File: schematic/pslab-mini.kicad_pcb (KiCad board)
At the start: 4 copper layers, 85 x 56 mm, 145 parts, among them J2 BAT, J3 Conn_Coaxial, J4 Conn_Coaxial, J5 Conn_02x16_Odd_Even, J6 Conn_01x15_Socket, J7 Conn_02x03_Top_Bottom, J8 USB_C_Receptacle_USB2.0_16P, Q1 MMBT3904, Q2 MMBT3906, SW1 Reset, SW2 Power, U1 MT2496, U10 TL082, U11 ESP32-C3, U12 IP5189T, U2 AP3015A, U4 SP0503BAHT, U5 AMS1117-3.3, U6 STM32H563RIT6, U7 TL082, U8 MCP6S21, U9 MCP6S21, X1 32kHz768, Y1 Crystal_25MHz, Y2 Crystal_40Mhz

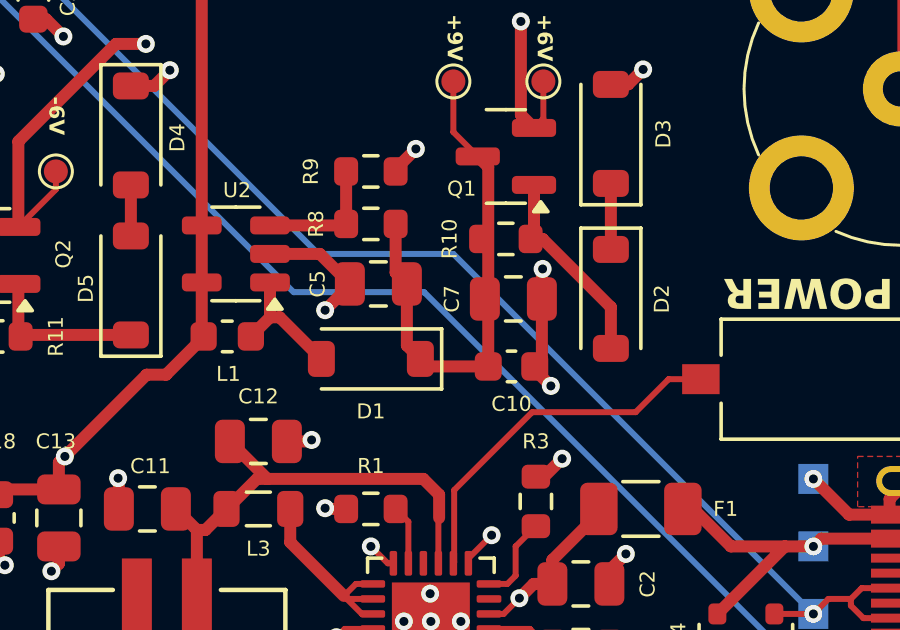
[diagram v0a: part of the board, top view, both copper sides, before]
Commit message: fix: wrong capacitor placement in voltage doubler
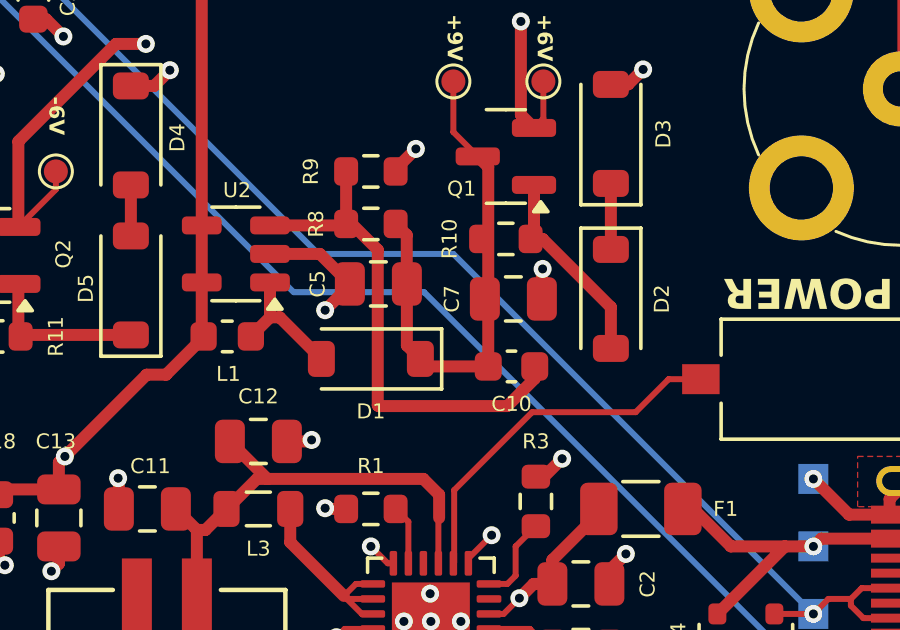
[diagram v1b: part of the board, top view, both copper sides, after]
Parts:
- D1: value K1N5817HW-7-F -> K1N5817HW
- D3: value 6.8V -> 6v8
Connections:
- C10 pad 2: GND -> Net-(U2-FB)
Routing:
- net Net-(U2-FB): track 4.31 -> 17.4 mm
- net GND: track 122.4 -> 119.2 mm, vias 84 -> 83

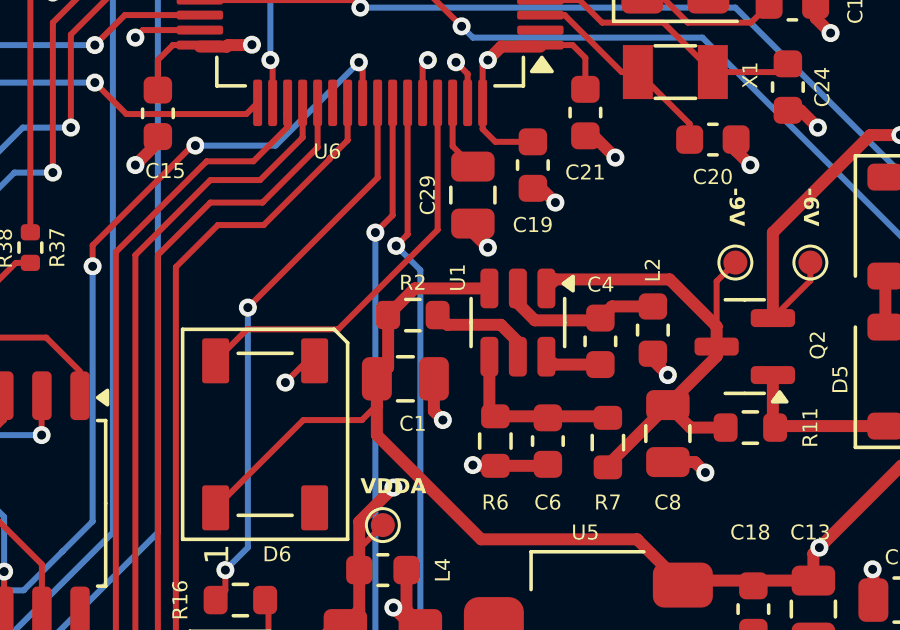
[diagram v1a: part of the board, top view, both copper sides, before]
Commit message: fix: schematic placement of voltage inverter block
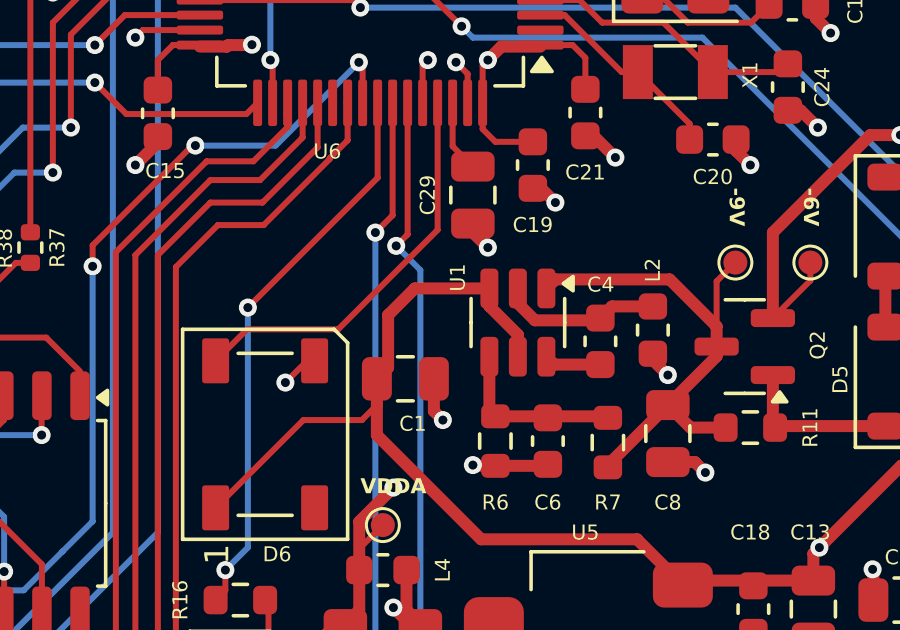
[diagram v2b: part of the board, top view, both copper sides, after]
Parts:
- removed R2: 200k, Resistor_SMD:R_0603_1608Metric
- D4: value 6.8V -> 6v8
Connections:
- U1 pad 5: Net-(U1-EN) -> +5V
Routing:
- net Net-(U1-EN): track 3.54 -> 0.00 mm
- net +5V: track 88.8 -> 91.5 mm

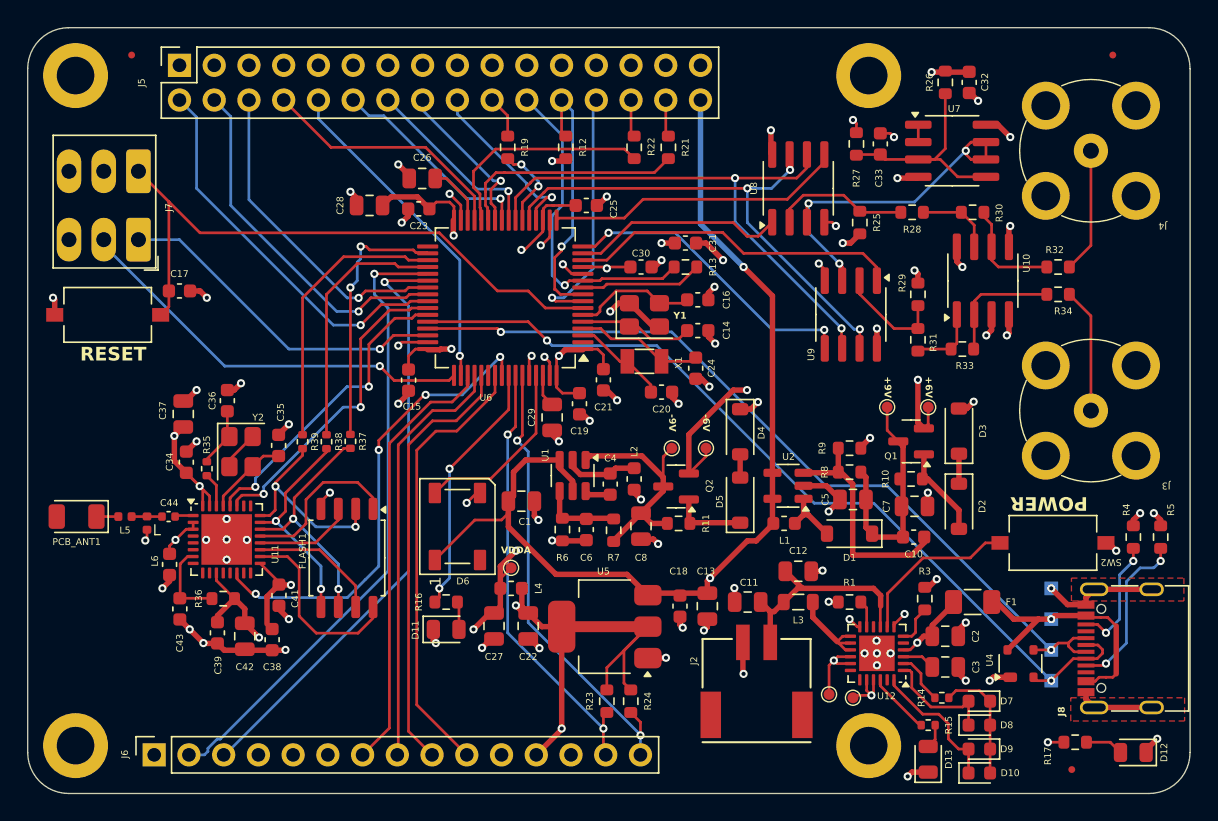
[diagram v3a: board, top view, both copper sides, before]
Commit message: Updated differential routing
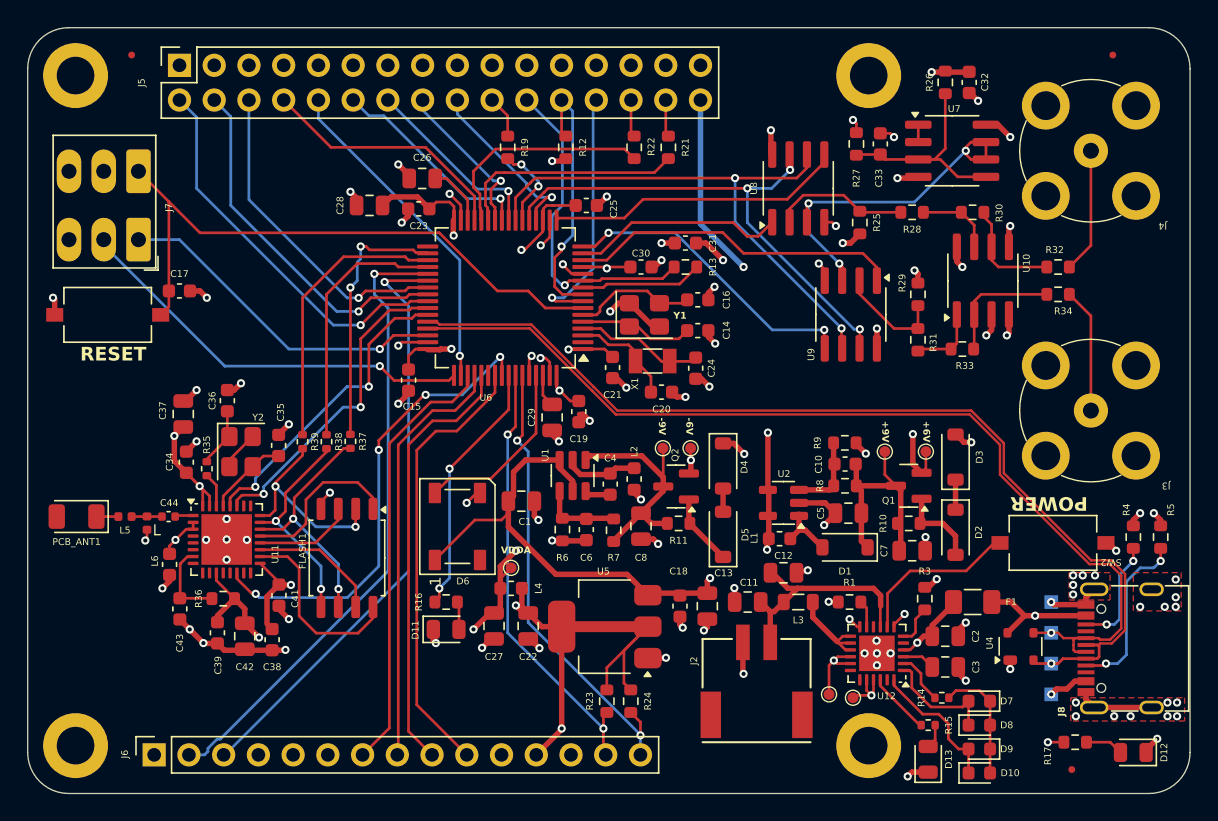
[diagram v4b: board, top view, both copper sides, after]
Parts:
- moved C10 7.33 mm to (139.4, 85.2), turned to 180 degrees
- moved TP2 5.50 mm to (154.5, 102.0)
- moved C7 3.25 mm to (144.3, 91.5)
- moved Q1 3.25 mm to (144.1, 86.8)
- moved R10 3.25 mm to (144.1, 89.5)
- moved TP7 3.25 mm to (142.3, 84.2)
- moved TP9 3.25 mm to (145.3, 84.2)
- moved D4 2.80 mm to (130.5, 85.3)
- moved D5 2.80 mm to (130.5, 90.3)
- moved D2 1.92 mm to (147.5, 90.2)
- moved D3 1.92 mm to (147.5, 84.7)
- moved U2 1.29 mm to (134.9, 88.0)
- moved TP4 1.25 mm to (154.5, 97.5)
- moved TP6 1.25 mm to (154.5, 99.8)
- moved U4 1.25 mm to (152.2, 98.5)
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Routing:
- net Net-(U2-FB): track 17.4 -> 5.88 mm
- net /D+: track 61.2 -> 72.2 mm, vias 2 -> 1
- net /D-: track 64.1 -> 74.2 mm, vias 2 -> 1
- net GND: track 119.2 -> 114.6 mm, vias 83 -> 101
- net -6V: track 55.1 -> 58.6 mm
- net +6V: track 35.2 -> 37.4 mm
- net +5V: track 91.5 -> 89.7 mm, vias 3 -> 5
- net VBUS: track 19.2 -> 18.3 mm, vias 1 -> 2
- net /LSE_IN: track 7.00 -> 7.76 mm
- net /BC_BATT: track 16.3 -> 17.0 mm
- net Net-(D2-A): track 6.84 -> 6.20 mm
- net Net-(J8-CC2): track 8.72 -> 8.21 mm
- net +3V3: track 218.4 -> 218.2 mm, vias 10 -> 11
